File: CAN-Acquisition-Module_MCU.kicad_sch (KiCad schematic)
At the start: 23 parts

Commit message: Finished CAN section
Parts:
- U?: value M483SGCAE2A -> M483SGCAE
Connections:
- net CAN_RX: now also U?.26 (PA.4)
- net CAN_TX: now also U?.25 (PA.5)
- net UART0_RX: now also U?.30 (PA.0); no longer U?.56 (PB.12)
- net UART0_TX: now also U?.29 (PA.1); no longer U?.55 (PB.13)
- net CAN_PIN8: now reaches U?.27 (PA.3)
- net CAN_PIN5: now reaches U?.28 (PA.2)
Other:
- note added: "2A variant has 2 ADCs. Not necessary, but can be used in case of shortage."
- note added: "CAN0"
- note added: "or M483SGCAE2A"
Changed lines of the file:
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@@
   (junction (at 190.5 118.11) (diameter 0) (color 0 0 0 0)
   )
+  (wire (pts (xy 180.34 85.09) (xy 182.88 85.09))
+    (stroke (width 0) (type default) (color 0 0 0 0))
+  )
   (wire (pts (xy 201.93 120.65) (xy 201.93 125.73))
     (stroke (width 0) (type default) (color 0 0 0 0))
@@
     (stroke (width 0) (type default) (color 0 0 0 0))
   )
-  (wire (pts (xy 116.84 90.17) (xy 124.46 90.17))
-    (stroke (width 0) (type default) (color 0 0 0 0))
-  )
   (wire (pts (xy 252.73 34.29) (xy 256.54 34.29))
     (stroke (width 0) (type default) (color 0 0 0 0))
@@
     (stroke (width 0) (type default) (color 0 0 0 0))
   )
+  (wire (pts (xy 180.34 87.63) (xy 182.88 87.63))
+    (stroke (width 0) (type default) (color 0 0 0 0))
+  )
   (wire (pts (xy 29.21 170.18) (xy 29.21 171.45))
     (stroke (width 0) (type default) (color 0 0 0 0))
@@
     (stroke (width 0) (type default) (color 0 0 0 0))
   )
-  (wire (pts (xy 181.61 74.93) (xy 180.34 74.93))
+  (wire (pts (xy 180.34 90.17) (xy 182.88 90.17))
+    (stroke (width 0) (type default) (color 0 0 0 0))
+  )
+  (wire (pts (xy 194.31 74.93) (xy 180.34 74.93))
     (stroke (width 0) (type default) (color 0 0 0 0))
   )
@@
     (stroke (width 0) (type default) (color 0 0 0 0))
   )
+  (wire (pts (xy 180.34 77.47) (xy 182.88 77.47))
+    (stroke (width 0) (type default) (color 0 0 0 0))
+  )
   (wire (pts (xy 114.3 173.99) (xy 114.3 175.26))
     (stroke (width 0) (type default) (color 0 0 0 0))
   )
-  (wire (pts (xy 124.46 87.63) (xy 116.84 87.63))
-    (stroke (width 0) (type default) (color 0 0 0 0))
-  )
   (wire (pts (xy 190.5 119.38) (xy 190.5 118.11))
     (stroke (width 0) (type default) (color 0 0 0 0))
@@
     (stroke (width 0) (type default) (color 0 0 0 0))
   )
+  (wire (pts (xy 182.88 80.01) (xy 180.34 80.01))
+    (stroke (width 0) (type default) (color 0 0 0 0))
+  )
   (wire (pts (xy 252.73 39.37) (xy 261.62 39.37))
     (stroke (width 0) (type default) (color 0 0 0 0))
@@
     (stroke (width 0) (type default) (color 0 0 0 0))
   )
+  (wire (pts (xy 180.34 82.55) (xy 182.88 82.55))
+    (stroke (width 0) (type default) (color 0 0 0 0))
+  )
   (wire (pts (xy 96.52 74.93) (xy 96.52 73.66))
     (stroke (width 0) (type default) (color 0 0 0 0))
   )
-  (wire (pts (xy 168.91 63.5) (xy 168.91 59.69))
+  (wire (pts (xy 168.91 63.5) (xy 168.91 60.96))
     (stroke (width 0) (type default) (color 0 0 0 0))
   )
@@
     (stroke (width 0) (type default) (color 0 0 0 0))
   )
-  (wire (pts (xy 171.45 63.5) (xy 171.45 59.69))
+  (wire (pts (xy 171.45 63.5) (xy 171.45 60.96))
     (stroke (width 0) (type default) (color 0 0 0 0))
   )
@@
     (stroke (width 0) (type default) (color 0 0 0 0))
   )
-  (wire (pts (xy 180.34 72.39) (xy 185.42 72.39))
+  (wire (pts (xy 180.34 72.39) (xy 182.88 72.39))
     (stroke (width 0) (type default) (color 0 0 0 0))
   )
@@
     (effects (font (size 1.4986 1.4986)) (justify left bottom))
   )
+  (text "2A variant has 2 ADCs. Not necessary, but can be used in case of shortage."
+    (at 193.04 165.1 0)
+    (effects (font (size 1.27 1.27)) (justify left bottom))
+  )
   (text "Verify that there are no CAN crossovers!" (at 66.04 29.21 0)
     (effects (font (size 3 3)) (justify left bottom))
@@
     (effects (font (size 2.9972 2.9972)) (justify left bottom))
   )
+  (text "or M483SGCAE2A" (at 146.05 95.25 0)
+    (effects (font (size 1 1) italic) (justify left bottom))
+  )
+  (text "CAN0" (at 191.77 90.17 0)
+    (effects (font (size 1.27 1.27)) (justify left bottom))
+  )
   (label "UART0_RX" (at 233.68 39.37 180)
     (effects (font (size 1.27 1.27)) (justify right bottom))
   )
-  (label "ICE_CLK" (at 168.91 59.69 90)
+  (label "ICE_CLK" (at 168.91 60.96 90)
     (effects (font (size 1.27 1.27)) (justify left bottom))
   )
@@
     (effects (font (size 1.27 1.27)) (justify left bottom))
   )
-  (label "ICE_DAT" (at 171.45 59.69 90)
+  (label "ICE_DAT" (at 171.45 60.96 90)
     (effects (font (size 1.27 1.27)) (justify left bottom))
   )
@@
     (effects (font (size 1.27 1.27)) (justify left bottom))
   )
-  (label "nRESET" (at 185.42 72.39 0)
+  (label "nRESET" (at 182.88 72.39 0)
     (effects (font (size 1.27 1.27)) (justify left bottom))
   )
-  (label "UART0_TX" (at 116.84 87.63 180)
-    (effects (font (size 1.27 1.27)) (justify right bottom))
+  (label "UART0_TX" (at 182.88 80.01 0)
+    (effects (font (size 1.27 1.27)) (justify left bottom))
   )
   (label "nRESET" (at 256.54 36.83 0)
     (effects (font (size 1.27 1.27)) (justify left bottom))
   )
-  (label "UART0_RX" (at 116.84 90.17 180)
-    (effects (font (size 1.27 1.27)) (justify right bottom))
+  (label "UART0_RX" (at 182.88 77.47 0)
+    (effects (font (size 1.27 1.27)) (justify left bottom))
   )
   (label "UART0_TX" (at 233.68 36.83 180)
     (effects (font (size 1.27 1.27)) (justify right bottom))
   )
-  (hierarchical_label "CAN_RX" (shape input) (at 96.52 35.56 180)
-    (effects (font (size 1.27 1.27)) (justify right))
-  )
-  (hierarchical_label "CAN_TX" (shape input) (at 96.52 33.02 180)
-    (effects (font (size 1.27 1.27)) (justify right))
+  (hierarchical_label "CAN_RX" (shape input) (at 182.88 87.63 0)
+    (effects (font (size 1.27 1.27)) (justify left))
+  )
+  (hierarchical_label "CAN_PIN5" (shape output) (at 182.88 82.55 0)
+    (effects (font (size 1.27 1.27)) (justify left))
+  )
+  (hierarchical_label "CAN_TX" (shape output) (at 182.88 90.17 0)
+    (effects (font (size 1.27 1.27)) (justify left))
+  )
+  (hierarchical_label "CAN_PIN8" (shape output) (at 182.88 85.09 0)
+    (effects (font (size 1.27 1.27)) (justify left))
   )
   (hierarchical_label "USB_VBUS" (shape input) (at 140.97 60.96 90)
@@
       (effects (font (size 1.27 1.27)) (justify left))
     )
-    (property "Value" "M483SGCAE2A" (id 1) (at 146.05 91.44 0)
+    (property "Value" "M483SGCAE" (id 1) (at 147.32 92.71 0)
       (effects (font (size 1.27 1.27)) (justify left))
     )
@@
     (pin "1")
   )
-  (symbol (lib_id "power:+3.3V") (at 181.61 74.93 270) (unit 1)
+  (symbol (lib_id "power:+3.3V") (at 194.31 74.93 270) (unit 1)
     (in_bom yes) (on_board yes) (fields_autoplaced)
-    (property "Reference" "#PWR?" (id 0) (at 177.8 74.93 0)
-      (effects (font (size 1.27 1.27)) hide)
-    )
-    (property "Value" "+3.3V" (id 1) (at 184.785 75.3638 90)
-      (effects (font (size 1.27 1.27)) (justify left))
-    )
-    (property "Footprint" "" (id 2) (at 181.61 74.93 0)
-      (effects (font (size 1.27 1.27)) hide)
-    )
-    (property "Datasheet" "" (id 3) (at 181.61 74.93 0)
-      (effects (font (size 1.27 1.27)) hide)
-    )
+    (property "Reference" "#PWR?" (id 0) (at 190.5 74.93 0)
+      (effects (font (size 1.27 1.27)) hide)
+    )
+    (property "Value" "+3.3V" (id 1) (at 197.485 75.3638 90)
+      (effects (font (size 1.27 1.27)) (justify left))
+    )
+    (property "Footprint" "" (id 2) (at 194.31 74.93 0)
+      (effects (font (size 1.27 1.27)) hide)
+    )
+    (property "Datasheet" "" (id 3) (at 194.31 74.93 0)
+      (effects (font (size 1.27 1.27)) hide)
+    )

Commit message: Added stuff and cleanup
Added LED, Power outputs, additional descriptions
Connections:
- net FAN_TACH: now reaches U?.10 (PA.9)
- net FAN_PWM_CTRL: now reaches U?.11 (PA.8)
- net POWER_OUT: now reaches U?.14 (PF.5)
- net LED_R: now reaches U?.53 (PB.15)
- net LED_G: now reaches U?.54 (PB.14)
- net LED_B: now reaches U?.55 (PB.13)
- net USB_ID renamed USB_OTG_ID
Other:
- note added: "BPWM0_CH3"
- note added: "CAN0_RXD"
- note added: "CAN0_TXD"
- note added: "Check programmer orientation!"
- note added: "ECAP0_IC1"
- note added: "EPWM0_CH0"
- note added: "EPWM1_CH0"
- note added: "EPWM1_CH1"
- note added: "EPWM1_CH2"
- note added: "PA.2"
- note added: "PA.3"
- note removed: "CAN0"
- note removed: "COM port/USB connector (?)"
- note removed: "Verify that there are no CAN crossovers!"
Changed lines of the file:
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@@
+    (stroke (width 0) (type default) (color 0 0 0 0))
+  )
+  (wire (pts (xy 121.92 87.63) (xy 124.46 87.63))
     (stroke (width 0) (type default) (color 0 0 0 0))
   )
@@
     (stroke (width 0) (type default) (color 0 0 0 0))
   )
+  (wire (pts (xy 156.21 119.38) (xy 156.21 121.92))
+    (stroke (width 0) (type default) (color 0 0 0 0))
+  )
   (wire (pts (xy 138.43 60.96) (xy 138.43 63.5))
     (stroke (width 0) (type default) (color 0 0 0 0))
@@
     (stroke (width 0) (type default) (color 0 0 0 0))
   )
+  (wire (pts (xy 158.75 119.38) (xy 158.75 121.92))
+    (stroke (width 0) (type default) (color 0 0 0 0))
+  )
   (wire (pts (xy 194.31 74.93) (xy 180.34 74.93))
     (stroke (width 0) (type default) (color 0 0 0 0))
@@
     (stroke (width 0) (type default) (color 0 0 0 0))
   )
+  (wire (pts (xy 121.92 82.55) (xy 124.46 82.55))
+    (stroke (width 0) (type default) (color 0 0 0 0))
+  )
   (wire (pts (xy 41.91 171.45) (xy 54.61 171.45))
     (stroke (width 0) (type default) (color 0 0 0 0))
@@
     (stroke (width 0) (type default) (color 0 0 0 0))
   )
+  (wire (pts (xy 166.37 119.38) (xy 166.37 121.92))
+    (stroke (width 0) (type default) (color 0 0 0 0))
+  )
   (wire (pts (xy 194.31 97.79) (xy 205.74 97.79))
     (stroke (width 0) (type default) (color 0 0 0 0))
@@
   )
   (wire (pts (xy 171.45 63.5) (xy 171.45 60.96))
+    (stroke (width 0) (type default) (color 0 0 0 0))
+  )
+  (wire (pts (xy 121.92 85.09) (xy 124.46 85.09))
     (stroke (width 0) (type default) (color 0 0 0 0))
   )
@@
     (effects (font (size 1.4986 1.4986)) (justify left bottom))
   )
+  (text "PA.3" (at 193.675 85.725 0)
+    (effects (font (size 1.27 1.27)) (justify left bottom))
+  )
   (text "Place next to pins 13, 23, 31 & 51" (at 30.48 184.15 0)
     (effects (font (size 1.4986 1.4986)) (justify left bottom))
@@
     (effects (font (size 1.27 1.27)) (justify left bottom))
   )
-  (text "Verify that there are no CAN crossovers!" (at 66.04 29.21 0)
+  (text "EPWM1_CH0" (at 102.87 83.185 0)
+    (effects (font (size 1.27 1.27)) (justify left bottom))
+  )
+  (text "ECAP0_IC1" (at 157.48 143.51 90)
+    (effects (font (size 1.27 1.27)) (justify left bottom))
+  )
+  (text "CAN0_RXD" (at 191.77 88.265 0)
+    (effects (font (size 1.27 1.27)) (justify left bottom))
+  )
+  (text "CAN0_TXD" (at 191.77 90.805 0)
+    (effects (font (size 1.27 1.27)) (justify left bottom))
+  )
+  (text "Check programmer orientation!" (at 219.71 54.61 0)
     (effects (font (size 3 3)) (justify left bottom))
+  )
+  (text "EPWM1_CH1" (at 102.87 85.725 0)
+    (effects (font (size 1.27 1.27)) (justify left bottom))
   )
   (text "Place next to pin 57" (at 115.57 187.96 0)
     (effects (font (size 1.4986 1.4986)) (justify left bottom))
   )
-  (text "COM port/USB connector (?)" (at 200.66 154.94 0)
-    (effects (font (size 2.9972 2.9972)) (justify left bottom))
+  (text "EPWM0_CH0" (at 167.64 146.05 90)
+    (effects (font (size 1.27 1.27)) (justify left bottom))
   )
   (text "or M483SGCAE2A" (at 146.05 95.25 0)
     (effects (font (size 1 1) italic) (justify left bottom))
   )
-  (text "CAN0" (at 191.77 90.17 0)
+  (text "BPWM0_CH3" (at 160.02 149.86 90)
+    (effects (font (size 1.27 1.27)) (justify left bottom))
+  )
+  (text "EPWM1_CH2" (at 102.87 88.265 0)
+    (effects (font (size 1.27 1.27)) (justify left bottom))
+  )
+  (text "PA.2" (at 193.675 83.185 0)
     (effects (font (size 1.27 1.27)) (justify left bottom))
   )
@@
     (effects (font (size 1.27 1.27)) (justify left))
   )
+  (hierarchical_label "POWER_OUT" (shape output) (at 166.37 121.92 270)
+    (effects (font (size 1.27 1.27)) (justify right))
+  )
   (hierarchical_label "CAN_PIN5" (shape output) (at 182.88 82.55 0)
     (effects (font (size 1.27 1.27)) (justify left))
@@
     (effects (font (size 1.27 1.27)) (justify left))
   )
+  (hierarchical_label "FAN_PWM_CTRL" (shape output) (at 158.75 121.92 270)
+    (effects (font (size 1.27 1.27)) (justify right))
+  )
   (hierarchical_label "CAN_PIN8" (shape output) (at 182.88 85.09 0)
     (effects (font (size 1.27 1.27)) (justify left))
@@
     (effects (font (size 1.27 1.27)) (justify left))
   )
-  (hierarchical_label "USB_D-" (shape input) (at 138.43 60.96 90)
+  (hierarchical_label "LED_R" (shape output) (at 121.92 82.55 180)
+    (effects (font (size 1.27 1.27)) (justify right))
+  )
+  (hierarchical_label "USB_D-" (shape bidirectional) (at 138.43 60.96 90)
     (effects (font (size 1.27 1.27)) (justify left))
   )
-  (hierarchical_label "USB_ID" (shape input) (at 133.35 60.96 90)
+  (hierarchical_label "LED_G" (shape output) (at 121.92 85.09 180)
+    (effects (font (size 1.27 1.27)) (justify right))
+  )
+  (hierarchical_label "USB_OTG_ID" (shape input) (at 133.35 60.96 90)
     (effects (font (size 1.27 1.27)) (justify left))
   )
-  (hierarchical_label "USB_D+" (shape input) (at 135.89 60.96 90)
+  (hierarchical_label "FAN_TACH" (shape input) (at 156.21 121.92 270)
+    (effects (font (size 1.27 1.27)) (justify right))
+  )
+  (hierarchical_label "USB_D+" (shape bidirectional) (at 135.89 60.96 90)
     (effects (font (size 1.27 1.27)) (justify left))
+  )
+  (hierarchical_label "LED_B" (shape output) (at 121.92 87.63 180)
+    (effects (font (size 1.27 1.27)) (justify right))
   )
   (symbol (lib_id "CAN-Acquisition-Module-rescue:M483SGCAE2A-CAN-Acquisition-Module") (at 127 66.04 0) (unit 1)
@@
   )
   (symbol (lib_id "power:+3.3V") (at 163.83 120.65 180) (unit 1)
-    (in_bom yes) (on_board yes) (fields_autoplaced)
+    (in_bom yes) (on_board yes)
     (property "Reference" "#PWR?" (id 0) (at 163.83 116.84 0)
       (effects (font (size 1.27 1.27)) hide)
     )
-    (property "Value" "+3.3V" (id 1) (at 163.83 125.0934 0))
+    (property "Value" "+3.3V" (id 1) (at 163.83 127 90))
     (property "Footprint" "" (id 2) (at 163.83 120.65 0)
       (effects (font (size 1.27 1.27)) hide)

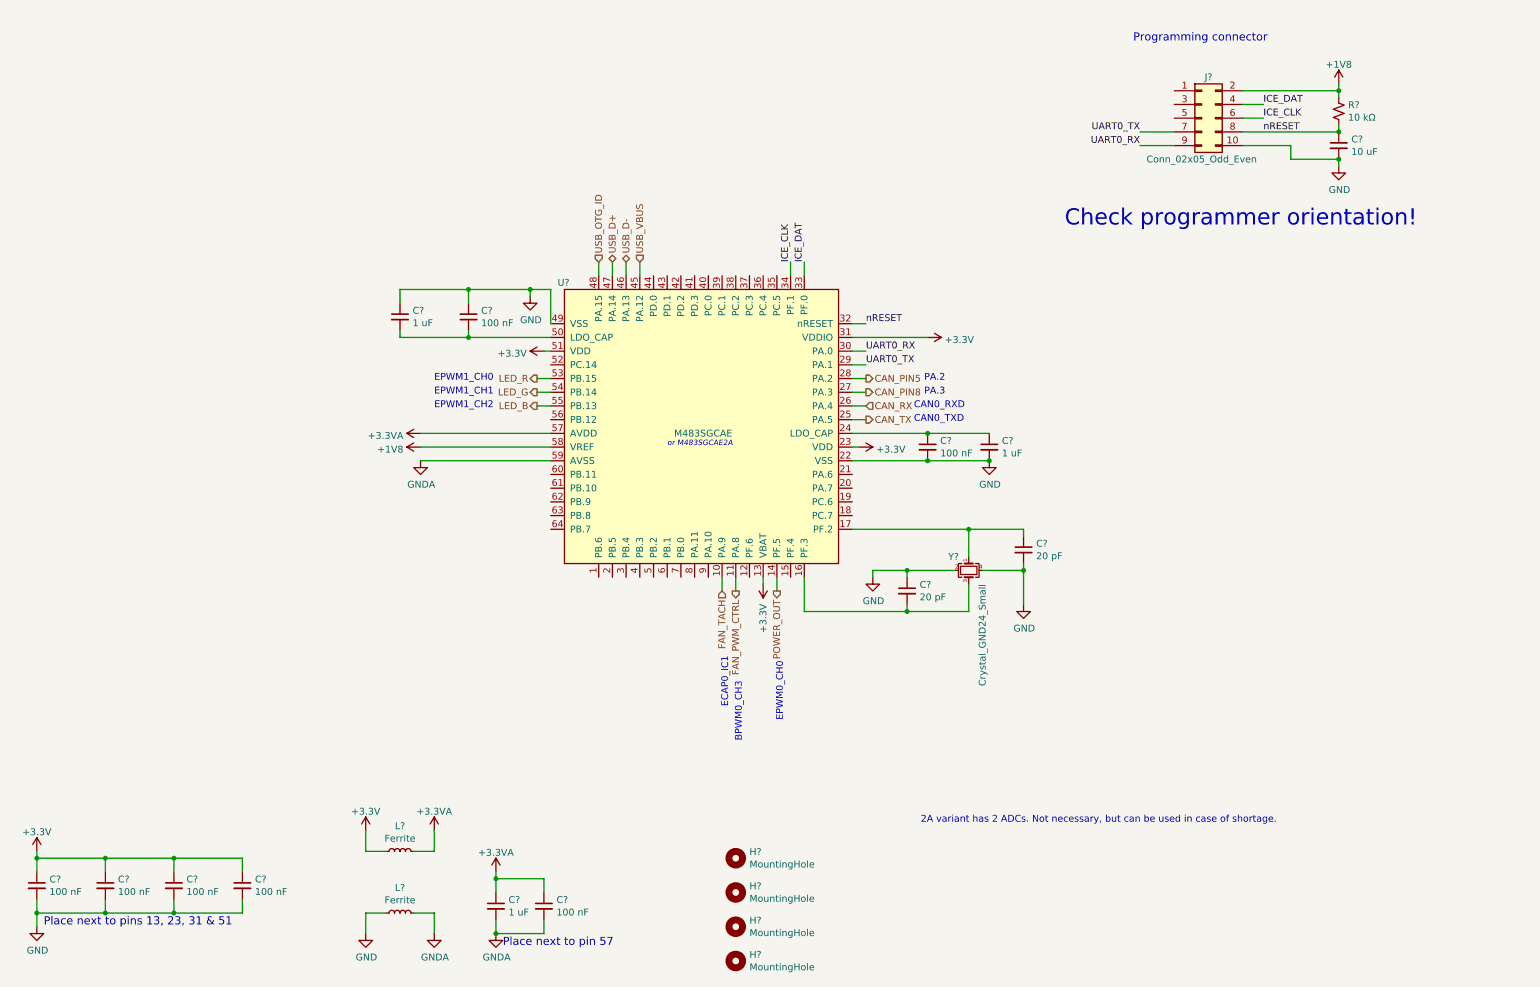
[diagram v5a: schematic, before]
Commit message: Added analog and sensors sections
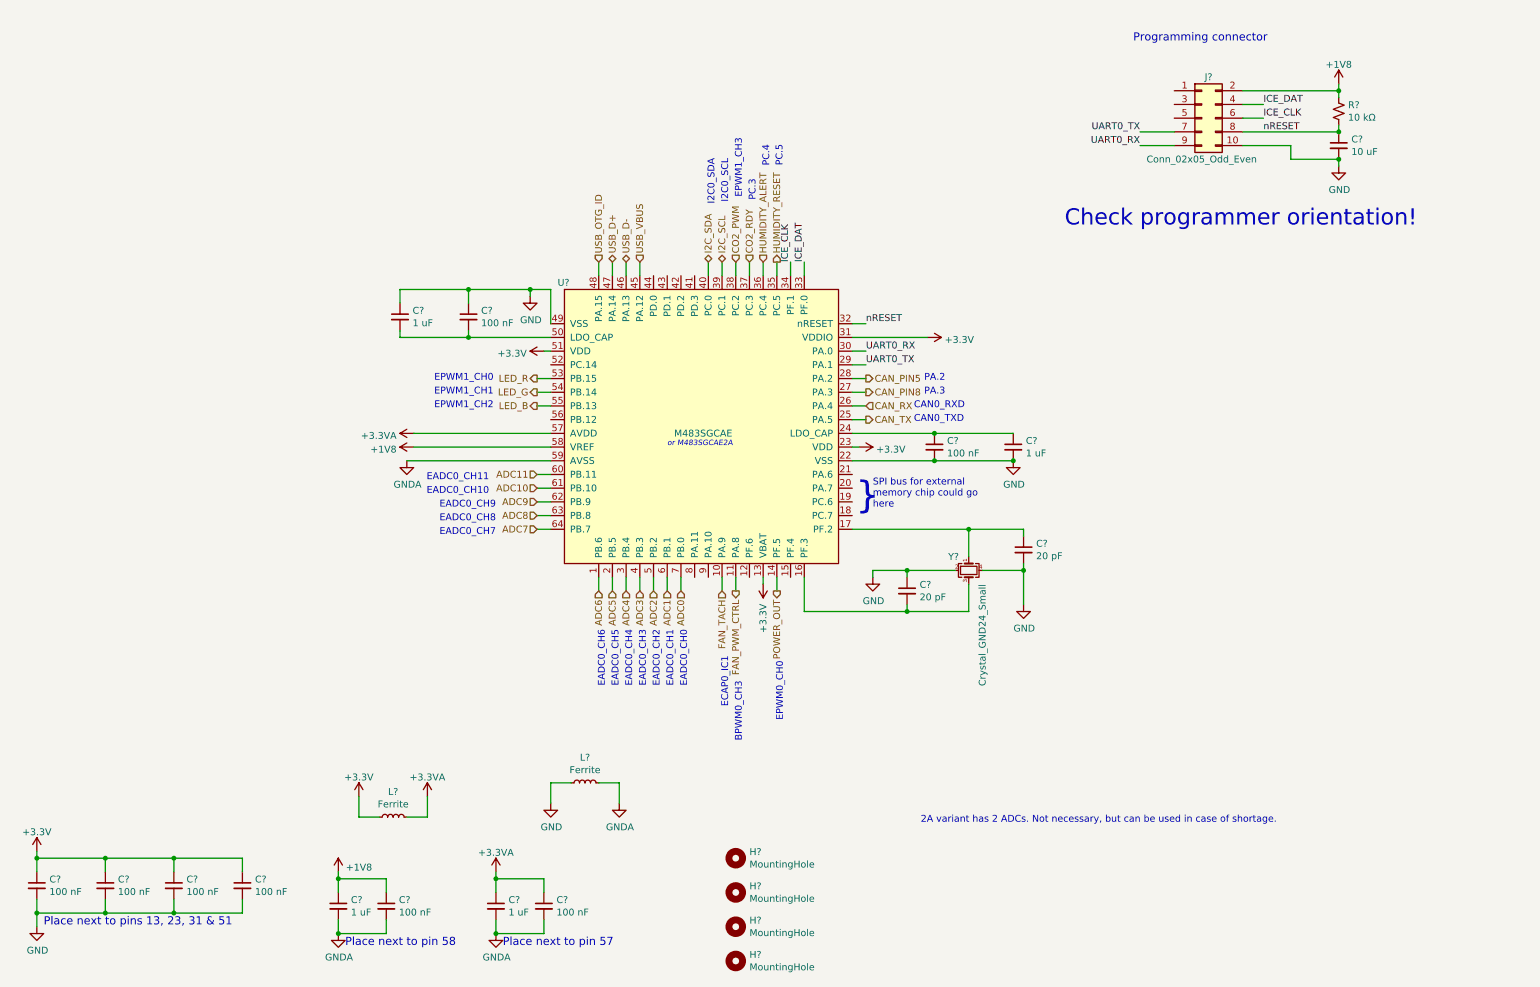
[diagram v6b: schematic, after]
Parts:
- added C?: 1 uF, Capacitor_SMD:C_0603_1608Metric, symbol Device:C_Small
- added C?: 100 nF, Capacitor_SMD:C_0402_1005Metric, symbol Device:C_Small
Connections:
- net +1V8: now also C?.1, C?.1
- net GNDA: now also C?.2, C?.2
- net ADC6: now reaches U?.1 (PB.6)
- net ADC5: now reaches U?.2 (PB.5)
- net ADC4: now reaches U?.3 (PB.4)
- net HUMIDITY_RESET: now reaches U?.35 (PC.5)
- net HUMIDITY_ALERT: now reaches U?.36 (PC.4)
- net CO2_RDY: now reaches U?.37 (PC.3)
- net CO2_PWM: now reaches U?.38 (PC.2)
- net I2C_SCL: now reaches U?.39 (PC.1)
- net ADC3: now reaches U?.4 (PB.3)
- net I2C_SDA: now reaches U?.40 (PC.0)
- net ADC2: now reaches U?.5 (PB.2)
- net ADC1: now reaches U?.6 (PB.1)
- net ADC11: now reaches U?.60 (PB.11)
- net ADC10: now reaches U?.61 (PB.10)
- net ADC9: now reaches U?.62 (PB.9)
- net ADC8: now reaches U?.63 (PB.8)
- net ADC7: now reaches U?.64 (PB.7)
- net ADC0: now reaches U?.7 (PB.0)
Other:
- note added: "EADC0_CH0"
- note added: "EADC0_CH1"
- note added: "EADC0_CH10"
- note added: "EADC0_CH11"
- note added: "EADC0_CH2"
- note added: "EADC0_CH3"
- note added: "EADC0_CH4"
- note added: "EADC0_CH5"
- note added: "EADC0_CH6"
- note added: "EADC0_CH7"
- note added: "EADC0_CH8"
- note added: "EADC0_CH9"
- note added: "EPWM1_CH3"
- note added: "I2C0_SCL"
- note added: "I2C0_SDA"
- note added: "PC.3"
- note added: "PC.4"
- note added: "PC.5"
- note added: "Place next to pin 58"
- note added: "SPI bus for external memory chip could go here"
- note added: "}"
- company: (none) -> École de Technologie Supérieure - Laboratoire thermique et science du bâtiment (LTSB)
- title: (none) -> CANbus Acquisition Module
- moved on the sheet: C?, L?
